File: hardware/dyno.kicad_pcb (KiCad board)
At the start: 2 copper layers, 21 parts, among them J1 Battery, J2 Load cell (4-wire), Q1 MMBT3906LT1G, SW1 B3U-1000P, U1 XIAO-ESP32-C3-SMD, U2 HX711

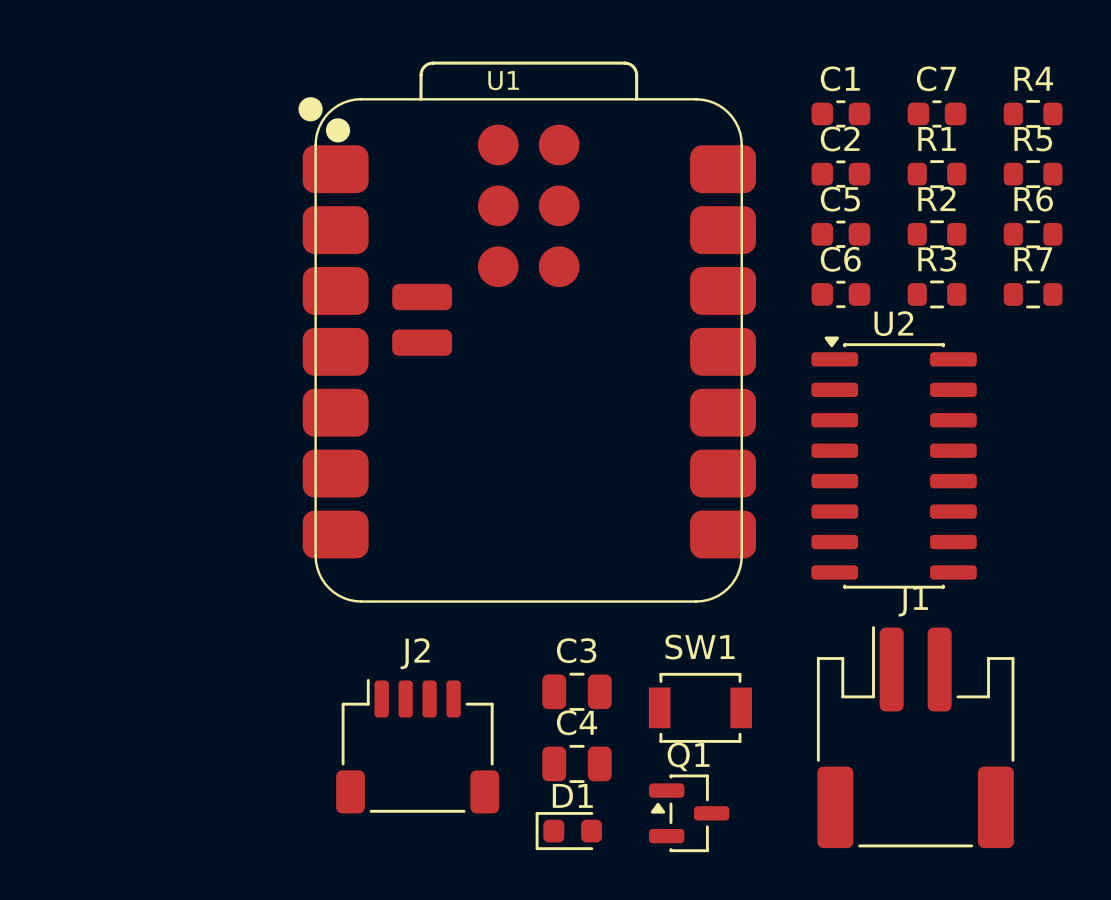
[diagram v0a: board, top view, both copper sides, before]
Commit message: Prepare hardware prototype for JLCPCB assembly
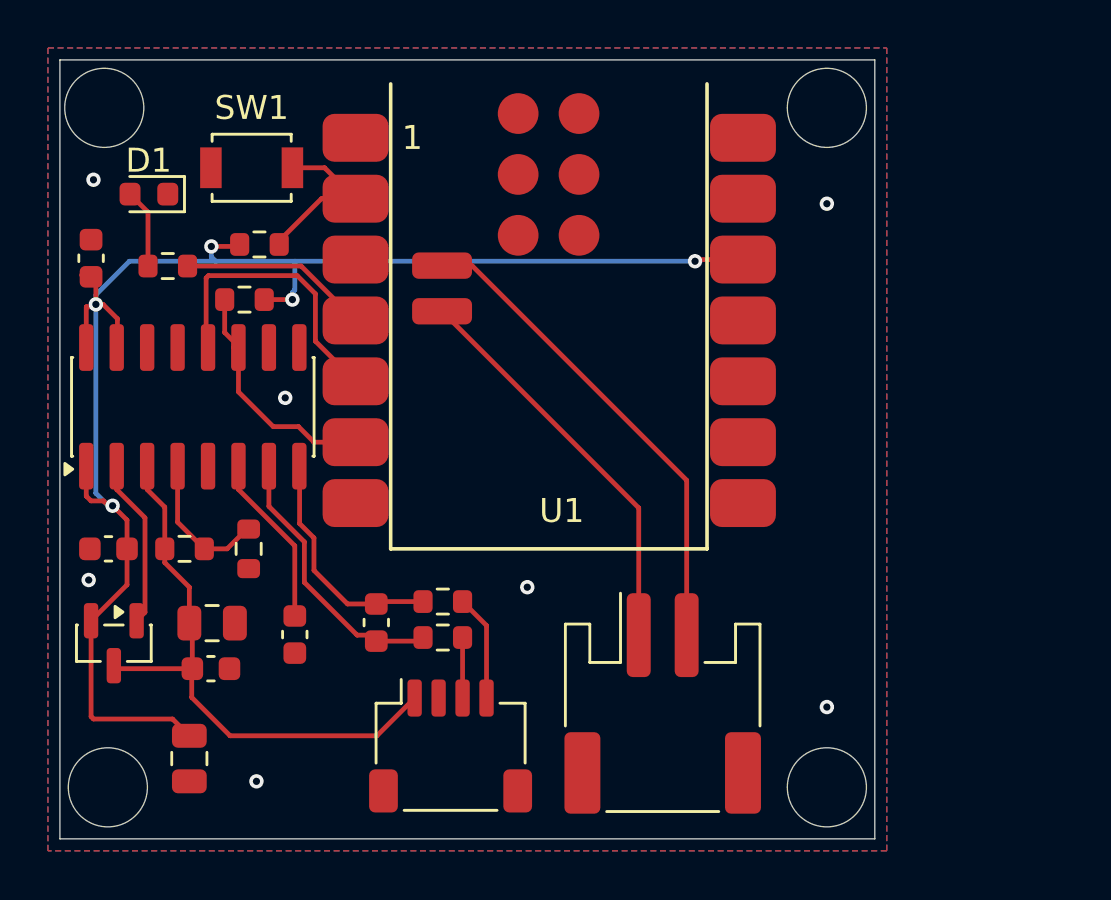
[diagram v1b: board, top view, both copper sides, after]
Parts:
- moved C7 39.0 mm to (81.5, 70.4)
- moved R4 37.4 mm to (87.4, 70.4), turned to -90 degrees
- moved R7 36.1 mm to (84.0, 58.6), turned to 180 degrees
- moved R3 33.1 mm to (84.7, 70.4)
- moved D1 31.9 mm to (83.2, 55.6), turned to 180 degrees
- moved C2 31.5 mm to (80.8, 58.3), turned to -90 degrees
- moved C1 31.5 mm to (89.3, 74.0), turned to -90 degrees
- moved R5 31.3 mm to (95.5, 74.1), turned to 180 degrees
- moved C6 30.6 mm to (85.8, 75.4)
- moved R1 29.4 mm to (87.2, 60.0)
- moved U2 29.4 mm to (85.0, 64.5), turned to 90 degrees
- moved SW1 29.3 mm to (87.5, 54.5)
- moved R6 29.0 mm to (95.5, 72.6), turned to 180 degrees
- moved R2 28.3 mm to (87.8, 57.7)
- moved C5 25.3 mm to (92.7, 73.5), turned to 90 degrees
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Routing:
- net +3V3: track 0.00 -> 64.2 mm, vias 0 -> 5
- net Net-(J2-Pin_1): track 0.00 -> 24.4 mm
- net Net-(J1-Pin_2): track 0.00 -> 20.4 mm
- net Net-(J1-Pin_1): track 0.00 -> 16.9 mm
- net /HX_DOUT: track 0.00 -> 12.2 mm
- net Net-(U2-INA-): track 0.00 -> 11.6 mm
- net /HX_SCK: track 0.00 -> 10.9 mm
- net Net-(U2-INA+): track 0.00 -> 9.77 mm
- net Net-(U1-D3): track 0.00 -> 7.95 mm
- net Net-(U1-D1): track 0.00 -> 7.23 mm
- net Net-(U2-VBG): track 0.00 -> 7.22 mm
- net Net-(Q1-B): track 0.00 -> 7.08 mm
- net Net-(U2-VFB): track 0.00 -> 5.75 mm
- net Net-(J2-Pin_4): track 0.00 -> 4.44 mm
- net Net-(D1-A): track 0.00 -> 3.31 mm
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- added copper zone on B.Cu, net GND
- added copper zone on F.Cu, net GND
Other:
- board outline added: 34 x 32.5 mm
- board text added: "1"
- board text added: "3 A- 4 A+"
- board text added: "DYNO PROTO 1"
- board text added: "J1: 1 BAT+ / 2 BAT-"
- board text added: "J2: 1 E+ 2 E-"
